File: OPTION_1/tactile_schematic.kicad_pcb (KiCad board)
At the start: 2 copper layers, 109.6 x 67.4 mm, 58 parts, among them IC1 CY8C4145PVI-PS431, J1 Conn_01x02, J2 Conn_01x04, J3 Conn_01x04, J4 Conn_01x02, J5 Conn_ARM_SWD_TagConnect_TC203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

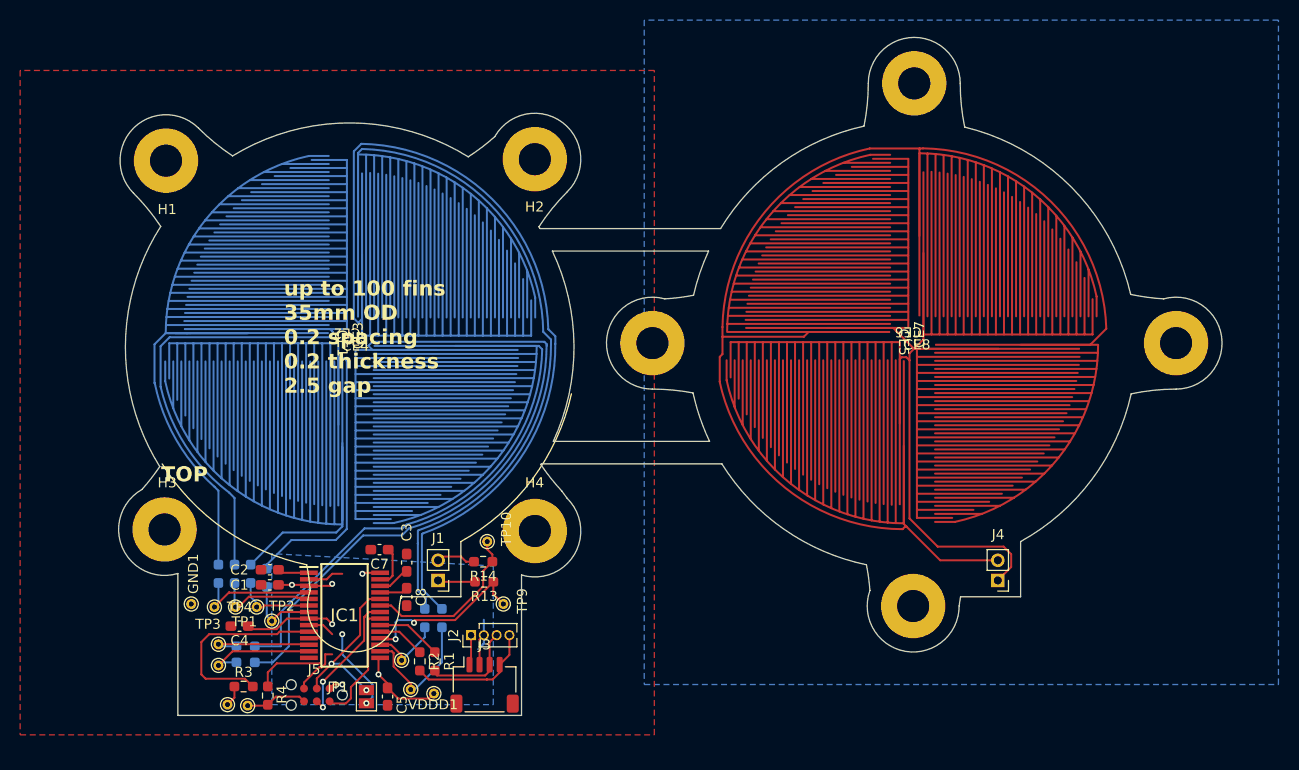
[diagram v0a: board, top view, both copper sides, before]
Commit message: - remove RST pad - change all resistors to 560ohm - remove UART test points - relayout with cleaning - conosolidate down to 3 capacitor values (replace 1uf w/ paralel 2 470ufs) - add power LED - move b2b connector to be more convinient to solder wire to - make shield driven from pin - add SHIELD to b2b connector
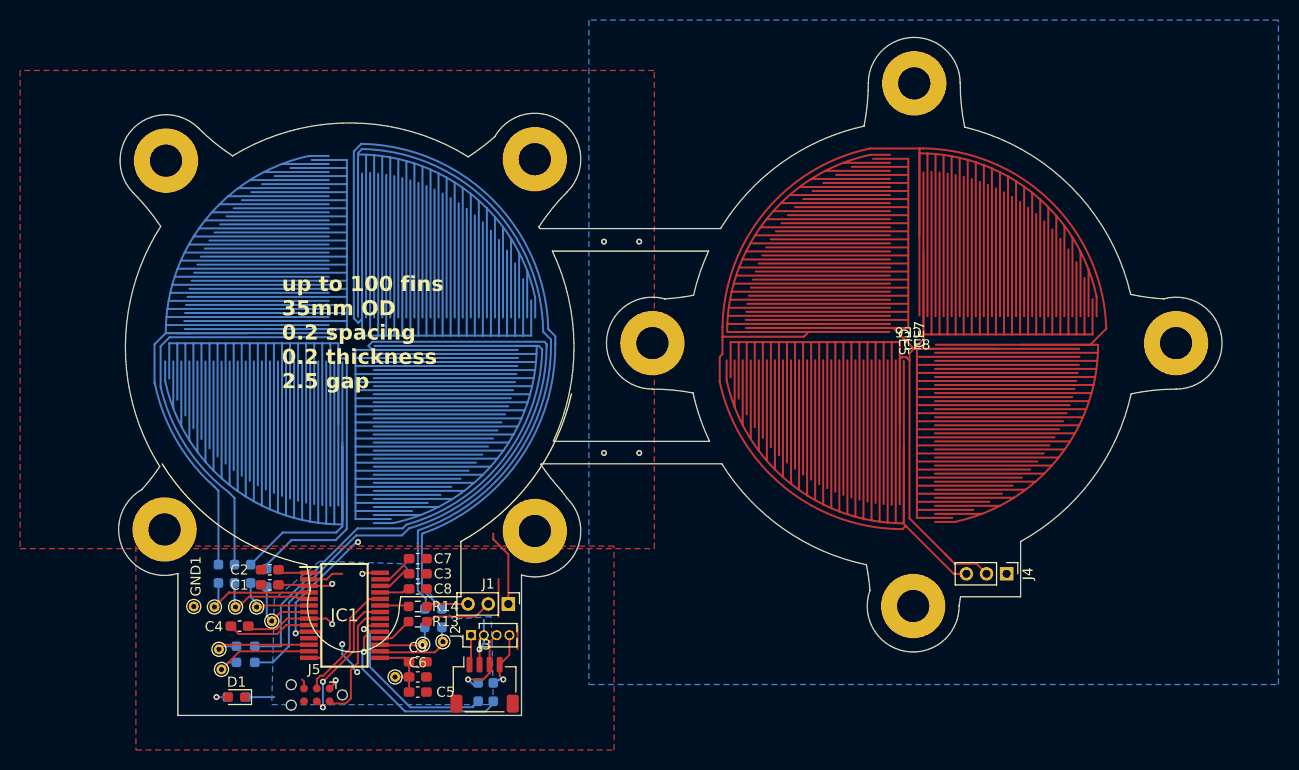
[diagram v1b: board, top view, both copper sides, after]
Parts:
- removed JP1: SolderJumper_2_Open, Jumper:SolderJumper-2_P1.3mm_Open_Pad1.0x1.5mm
- removed R4: 330, Resistor_SMD:R_0603_1608Metric_Pad0.98x0.95mm_HandSolder
- removed TP10, TP11, TP12, TP9: TestPoint, TestPoint:TestPoint_THTPad_D1.0mm_Drill0.5mm
- added C6: 470n, Capacitor_SMD:C_0603_1608Metric_Pad1.08x0.95mm_HandSolder, F.Cu at (193.5, 84.2)
- added C9: 0.1uF, Capacitor_SMD:C_0603_1608Metric_Pad1.08x0.95mm_HandSolder, F.Cu at (193.5, 82.8)
- added D1: LED, LED_SMD:LED_0603_1608Metric, F.Cu at (175.5, 86.2)
- C5: value 1uF -> 470n
- J1, J4: value Conn_01x02 -> Conn_01x03; footprint Connector_PinHeader_2.00mm:PinHeader_1x02_P2.00mm_Vertical -> Connector_PinHeader_2.00mm:PinHeader_1x03_P2.00mm_Vertical
- R1, R2, R3: value 330 -> 560; moved to B.Cu
- moved R2 7.91 mm to (201.0, 85.8), turned to 90 degrees
- moved R14 7.88 mm to (193.5, 77.2), turned to 0 degrees
- moved R13 7.69 mm to (193.5, 78.8), turned to 0 degrees
- moved J1 7.37 mm to (202.5, 77.0), turned to -90 degrees
- moved TP5 5.73 mm to (196.0, 80.8)
- moved R1 5.27 mm to (199.5, 85.8), turned to 90 degrees
- moved VDDD1 4.19 mm to (191.2, 84.2)
- moved C7 3.91 mm to (193.5, 72.5), turned to 0 degrees
- moved C5 3.03 mm to (193.5, 85.8), turned to 0 degrees
- moved TP6 2.64 mm to (194.0, 81.0)
- moved C3 1.56 mm to (193.5, 74.0), turned to 0 degrees
- moved C8 1.36 mm to (193.5, 75.5), turned to 0 degrees
- moved R3 1.26 mm to (175.5, 86.2), turned to 180 degrees
- moved J4 1.10 mm to (252.0, 74.0), turned to -90 degrees
- moved TP8 0.50 mm to (173.8, 81.5)
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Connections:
- CE5 pad 1: Net-(J1-Pin_1) -> Net-(J1-Pin_2)
- CE5 pad 2: Net-(J1-Pin_2) -> Net-(J1-Pin_3)
- CE6 pad 1: Net-(J1-Pin_1) -> Net-(J1-Pin_2)
- CE6 pad 2: Net-(J1-Pin_2) -> Net-(J1-Pin_3)
- CE7 pad 1: Net-(J1-Pin_1) -> Net-(J1-Pin_2)
- CE7 pad 2: Net-(J1-Pin_2) -> Net-(J1-Pin_3)
- CE8 pad 1: Net-(J1-Pin_1) -> Net-(J1-Pin_2)
- CE8 pad 2: Net-(J1-Pin_2) -> Net-(J1-Pin_3)
- IC1 pad 10: Net-(IC1-P2.0) -> SHEILD
- IC1 pad 11: Net-(IC1-P2.1) -> unconnected-(IC1-P2.1-Pad11)
- IC1 pad 14: unconnected-(IC1-P2.7/VREF-Pad14) -> SHEILD
- J1 pad 1: Net-(J1-Pin_1) -> SHEILD
- J4 pad 1: Net-(J1-Pin_1) -> SHEILD
- J5 pad 6: /UART_TX -> unconnected-(J5-SWO-Pad6)
- R13 pad 2: Net-(J1-Pin_1) -> Net-(J1-Pin_2)
- R14 pad 2: Net-(J1-Pin_2) -> Net-(J1-Pin_3)
- R3 pad 1: /UART_RX -> VDD
- R3 pad 2: Net-(IC1-P2.0) -> Net-(D1-A)
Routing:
- net Net-(J1-Pin_1): track 70.9 -> 0.00 mm
- net Net-(J1-Pin_3): track 0.00 -> 58.2 mm
- net SHEILD: track 0.00 -> 25.6 mm, vias 0 -> 6
- net Net-(IC1-P2.0): track 19.9 -> 0.00 mm
- net Net-(IC1-P3.6): track 4.87 -> 20.2 mm, vias 0 -> 1
- net CAP0A: track 17.6 -> 3.41 mm, vias 2 -> 0
- net CAP0B: track 16.9 -> 2.97 mm
- net Net-(IC1-P3.7): track 6.55 -> 18.7 mm, vias 0 -> 1
- net Net-(IC1-P2.1): track 10.6 -> 0.00 mm
- net Net-(J1-Pin_2): track 60.5 -> 70.1 mm
- net SCL: track 12.7 -> 6.19 mm, vias 0 -> 1
- net /UART_TX: track 6.16 -> 0.00 mm
- net CAP3A: track 13.3 -> 8.34 mm
- net /RESET: track 16.7 -> 12.3 mm, vias 2 -> 0
- net GND: track 22.7 -> 25.4 mm
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- added copper zone on B.Cu, net SHEILD
- added copper zone on F.Cu, net SHEILD
- removed copper zone on B.Cu, net GND
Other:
- board text removed: "BOTTOM"
- board text removed: "TOP"
